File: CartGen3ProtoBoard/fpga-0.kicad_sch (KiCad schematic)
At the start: 3 parts, among them J4 J3_Header, J5 J4_Header, J6 J6_Header

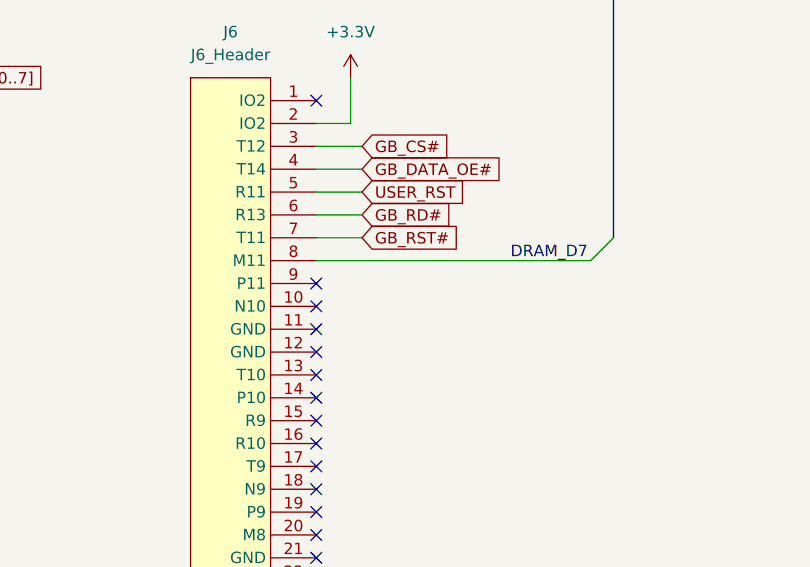
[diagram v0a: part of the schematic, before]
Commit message: Added audio schematic
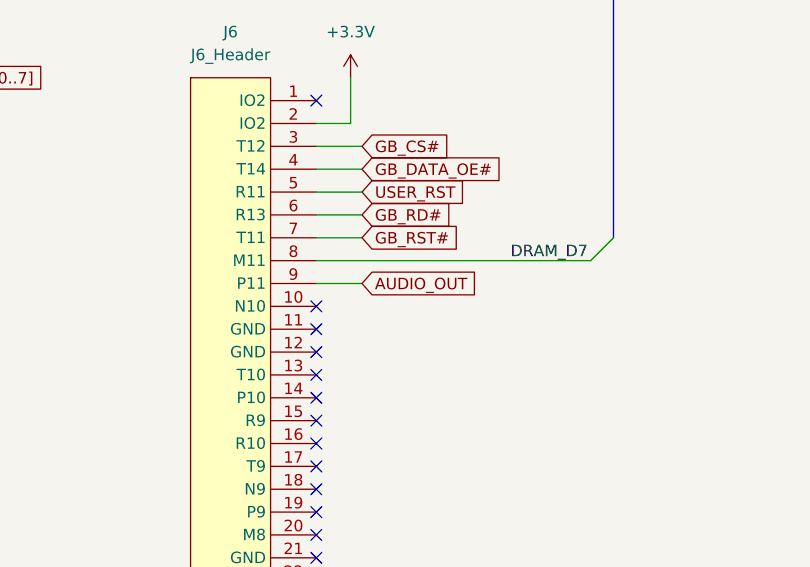
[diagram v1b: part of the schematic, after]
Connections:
- net AUDIO_OUT: now reaches J6.9 (P11)
- no-connect marks 54 -> 53
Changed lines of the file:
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@@
   (no_connect (at 227.33 72.39))
   (no_connect (at 227.33 69.85))
-  (no_connect (at 227.33 67.31))
   (no_connect (at 227.33 97.79))
   (no_connect (at 227.33 100.33))
@@
     (stroke (width 0) (type default) (color 0 0 0 0))
   )
+  (wire (pts (xy 227.33 67.31) (xy 232.41 67.31))
+    (stroke (width 0) (type default) (color 0 0 0 0))
+  )
   (wire (pts (xy 57.15 140.97) (xy 90.17 140.97))
     (stroke (width 0) (type default) (color 0 0 0 0))
@@
       (effects (font (size 1.27 1.27)) (justify left) hide)
     )
+  )
+  (global_label "AUDIO_OUT" (shape input) (at 232.41 67.31 0) (fields_autoplaced)
+    (effects (font (size 1.27 1.27)) (justify left))
+    (property "Intersheet References" "${INTERSHEET_REFS}" (id 0) (at 245.0436 67.2306 0)
+      (effects (font (size 1.27 1.27)) (justify left) hide)
+    )
